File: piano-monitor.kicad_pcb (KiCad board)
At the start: 2 copper layers, 37.2 x 43 mm, 1 part

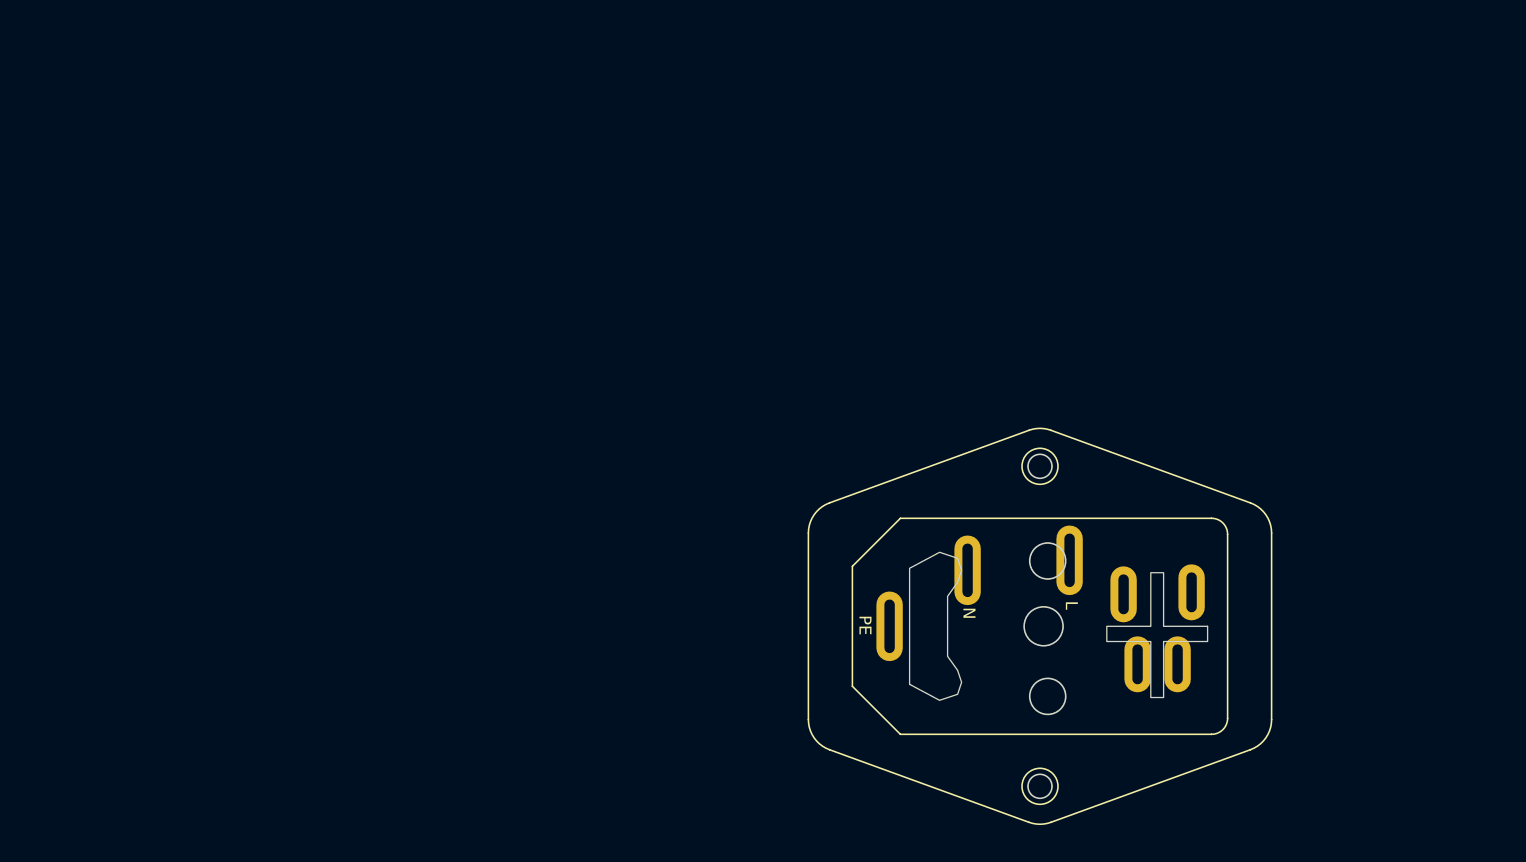
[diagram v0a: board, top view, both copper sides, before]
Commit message: Add tpa3110 footprint
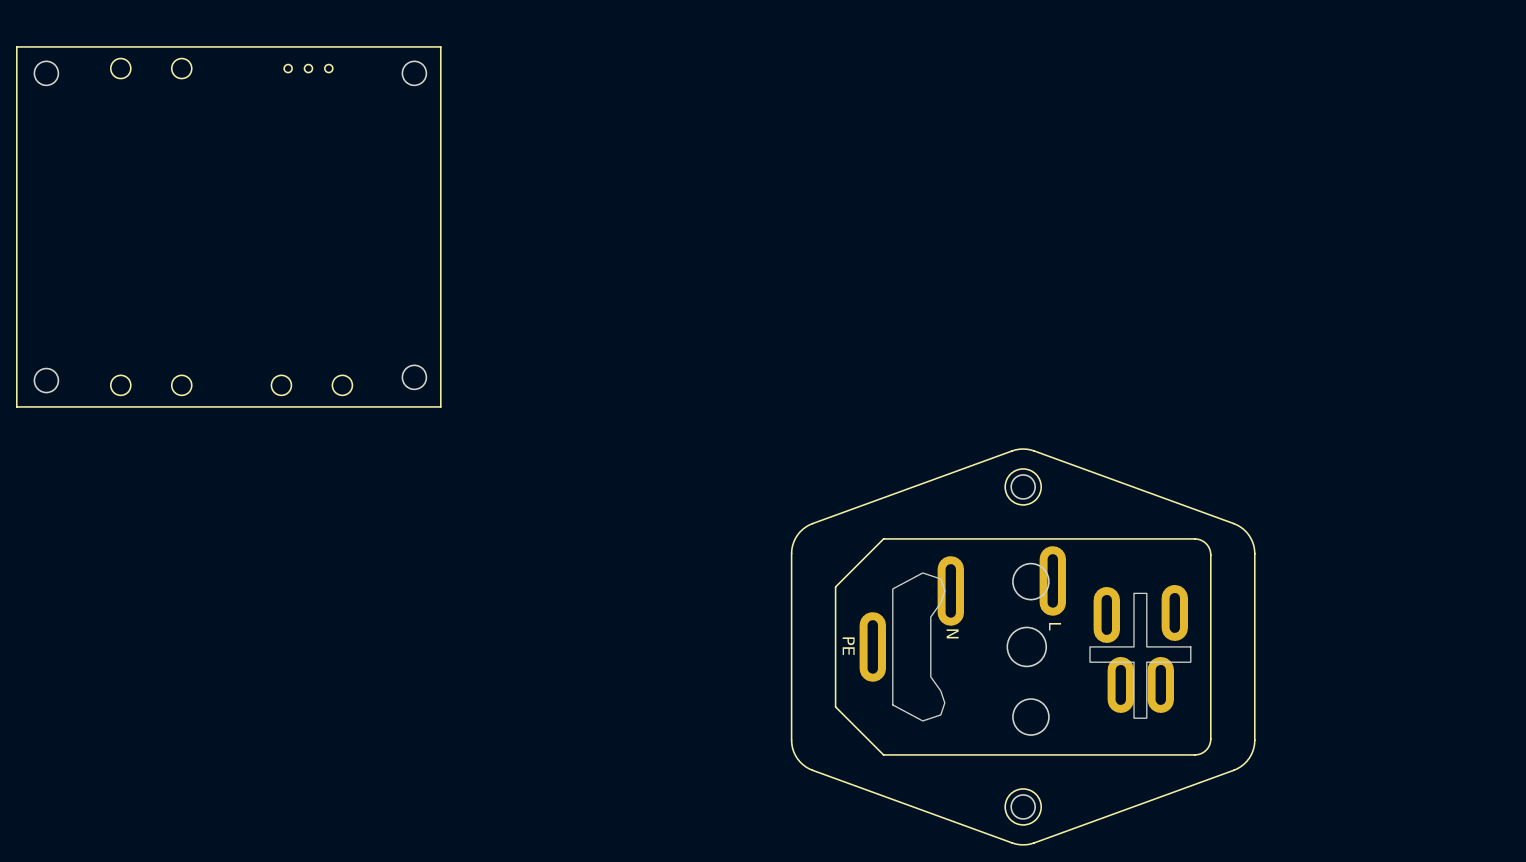
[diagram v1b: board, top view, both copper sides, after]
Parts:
- moved J1 3.33 mm to (224.2, 127.6)
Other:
- board size 37.2 x 43 mm -> 49 x 41.4 mm
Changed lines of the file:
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@@
 	(footprint "iec320-c14:iec320-c14"
 		(layer "F.Cu")
-		(at 226.25 125 -90)
+		(at 224.15 127.58 -90)
 		(property "Reference" "J1"
 			(at 0 -0.5 -90)
@@
 		)
 	)
+	(gr_line
+		(start 97.9 52.58)
+		(end 150.9 52.58)
+		(stroke
+			(width 0.2)
+			(type default)
+		)
+		(layer "F.SilkS")
+	)
+	(gr_circle
+		(center 118.52 55.28)
+		(end 119.77 55.28)
+		(stroke
+			(width 0.2)
+			(type default)
+		)
+		(fill none)
+		(layer "F.SilkS")
+	)
+	(gr_circle
+		(center 118.52 94.88)
+		(end 119.77 94.88)
+		(stroke
+			(width 0.2)
+			(type default)
+		)
+		(fill none)
+		(layer "F.SilkS")
+	)
+	(gr_line
+		(start 150.9 52.58)
+		(end 150.9 97.58)
+		(stroke
+			(width 0.2)
+			(type default)
+		)
+		(layer "F.SilkS")
+	)
+	(gr_circle
+		(center 136.9 55.28)
+		(end 137.4 55.28)
+		(stroke
+			(width 0.2)
+			(type default)
+		)
+		(fill none)
+		(layer "F.SilkS")
+	)
+	(gr_circle
+		(center 110.9 94.88)
+		(end 112.15 94.88)
+		(stroke
+			(width 0.2)
+			(type default)
+		)
+		(fill none)
+		(layer "F.SilkS")
+	)
+	(gr_circle
+		(center 131.82 55.28)
+		(end 132.32 55.28)
+		(stroke
+			(width 0.2)
+			(type default)
+		)
+		(fill none)
+		(layer "F.SilkS")
+	)
+	(gr_circle
+		(center 130.98 94.88)
+		(end 132.23 94.88)
+		(stroke
+			(width 0.2)
+			(type default)
+		)
+		(fill none)
+		(layer "F.SilkS")
+	)
+	(gr_circle
+		(center 138.6 94.88)
+		(end 139.85 94.88)
+		(stroke
+			(width 0.2)
+			(type default)
+		)
+		(fill none)
+		(layer "F.SilkS")
+	)
+	(gr_line
+		(start 150.9 97.58)
+		(end 97.9 97.58)
+		(stroke
+			(width 0.2)
+			(type default)
+		)
+		(layer "F.SilkS")
+	)
+	(gr_circle
+		(center 134.36 55.28)
+		(end 134.86 55.28)
+		(stroke
+			(width 0.2)
+			(type default)
+		)
+		(fill none)
+		(layer "F.SilkS")
+	)
+	(gr_circle
+		(center 124.4 75.08)
+		(end 124.41 75.08)
+		(stroke
+			(width 0.0001)
+			(type default)
+		)
+		(fill solid)
+		(layer "F.SilkS")
+	)
+	(gr_line
+		(start 97.9 97.58)
+		(end 97.9 52.58)
+		(stroke
+			(width 0.2)
+			(type default)
+		)
+		(layer "F.SilkS")
+	)
+	(gr_circle
+		(center 110.9 55.28)
+		(end 112.15 55.28)
+		(stroke
+			(width 0.2)
+			(type default)
+		)
+		(fill none)
+		(layer "F.SilkS")
+	)
+	(gr_circle
+		(center 147.6 93.88)
+		(end 149.1 93.88)
+		(stroke
+			(width 0.2)
+			(type default)
+		)
+		(fill none)
+		(layer "Edge.Cuts")
+	)
+	(gr_circle
+		(center 147.6 55.88)
+		(end 149.1 55.88)
+		(stroke
+			(width 0.2)
+			(type default)
+		)
+		(fill none)
+		(layer "Edge.Cuts")
+	)
+	(gr_circle
+		(center 101.6 94.28)
+		(end 103.1 94.28)
+		(stroke
+			(width 0.2)
+			(type default)
+		)
+		(fill none)
+		(layer "Edge.Cuts")
+	)
+	(gr_circle
+		(center 101.6 55.88)
+		(end 103.1 55.88)
+		(stroke
+			(width 0.2)
+			(type default)
+		)
+		(fill none)
+		(layer "Edge.Cuts")
+	)
 )

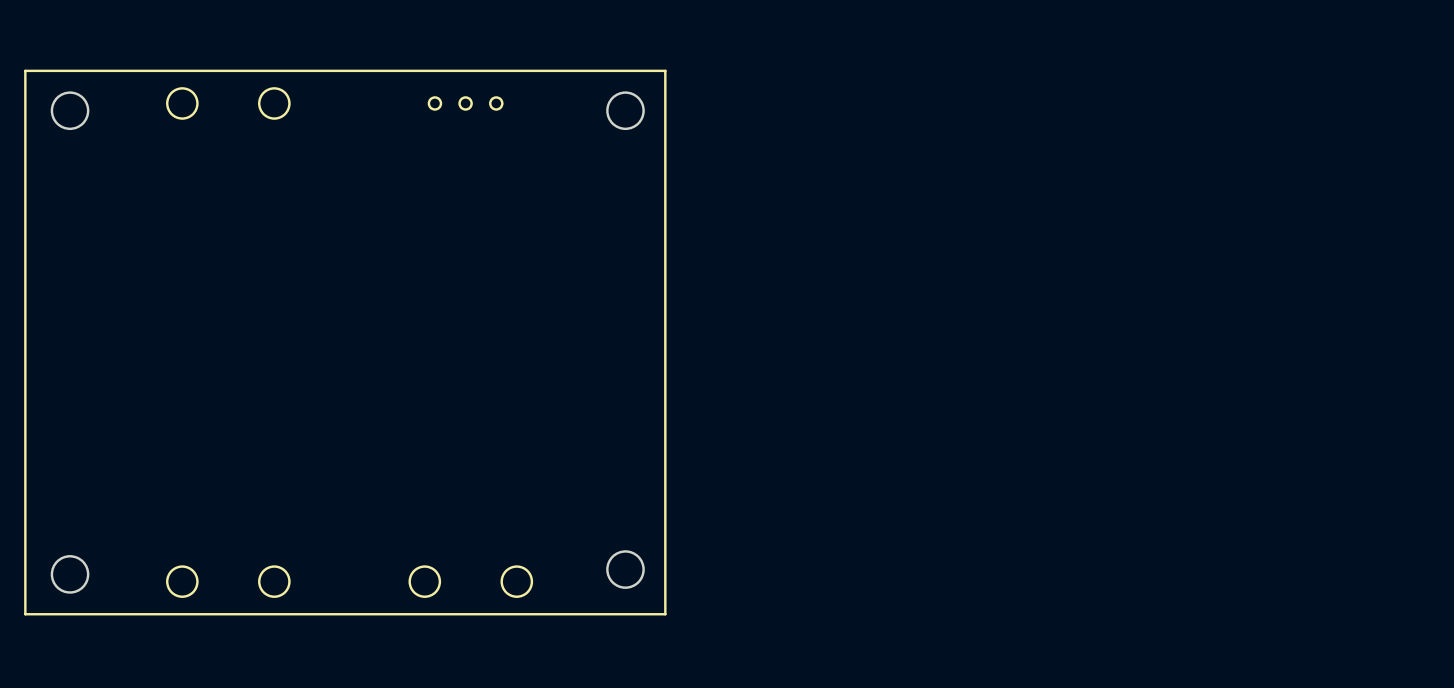
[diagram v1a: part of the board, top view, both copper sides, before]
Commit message: Add initial schematic
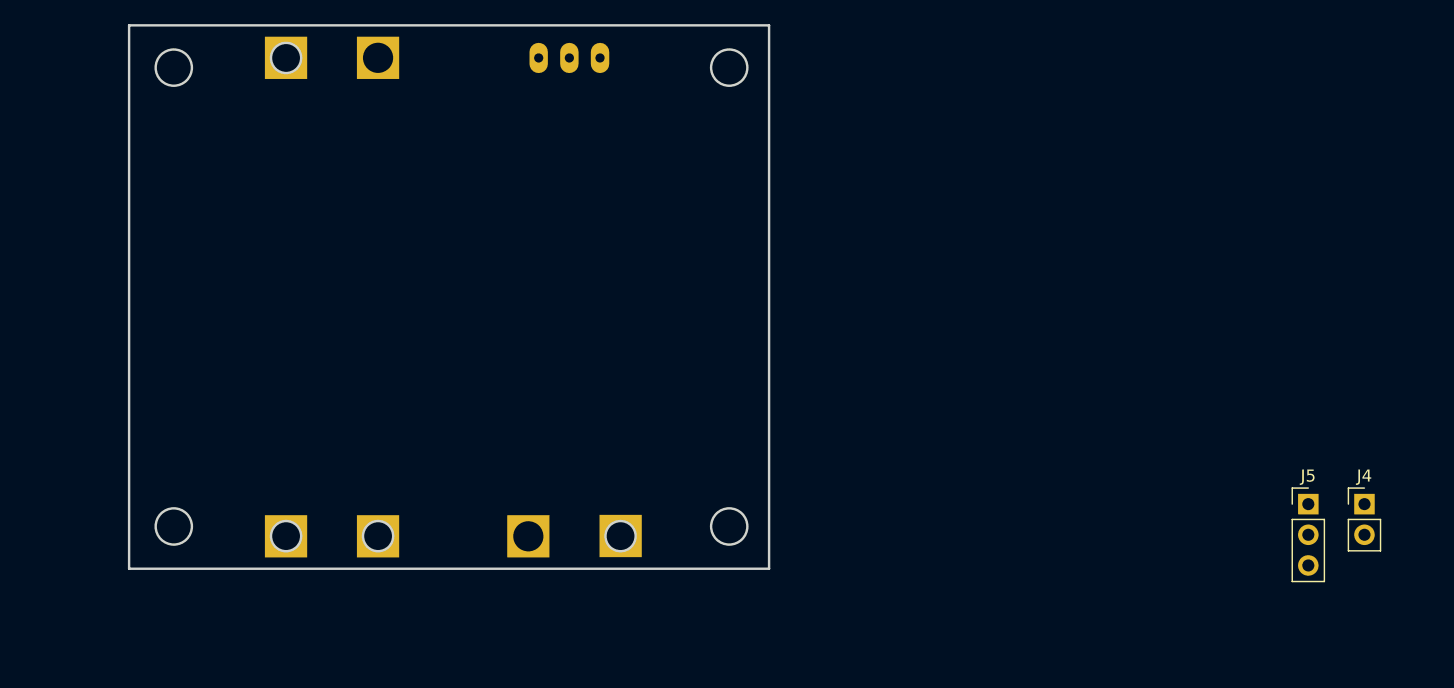
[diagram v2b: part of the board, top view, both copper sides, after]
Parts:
- added J4: DC, Connector_PinHeader_2.54mm:PinHeader_1x02_P2.54mm_Vertical, F.Cu at (208.8, 88.5)
- added J5: 230AC, Connector_PinHeader_2.54mm:PinHeader_1x03_P2.54mm_Vertical, F.Cu at (204.2, 88.5)
- added U1: ~, tpa3110:tpa3110, F.Cu at (133.0, 71.2)
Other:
- board size 49 x 41.4 mm -> 53 x 45 mm

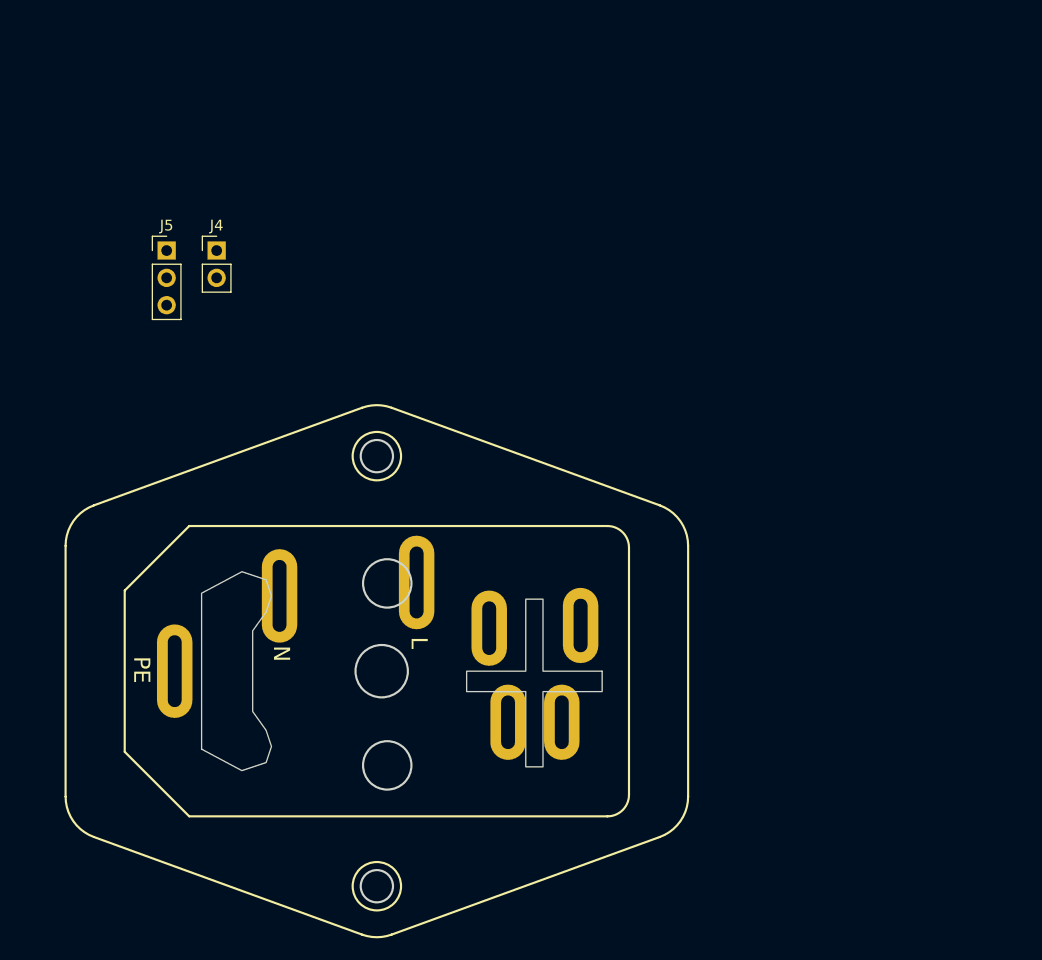
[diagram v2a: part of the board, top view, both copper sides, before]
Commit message: Update the C14 plug symbol and footprint
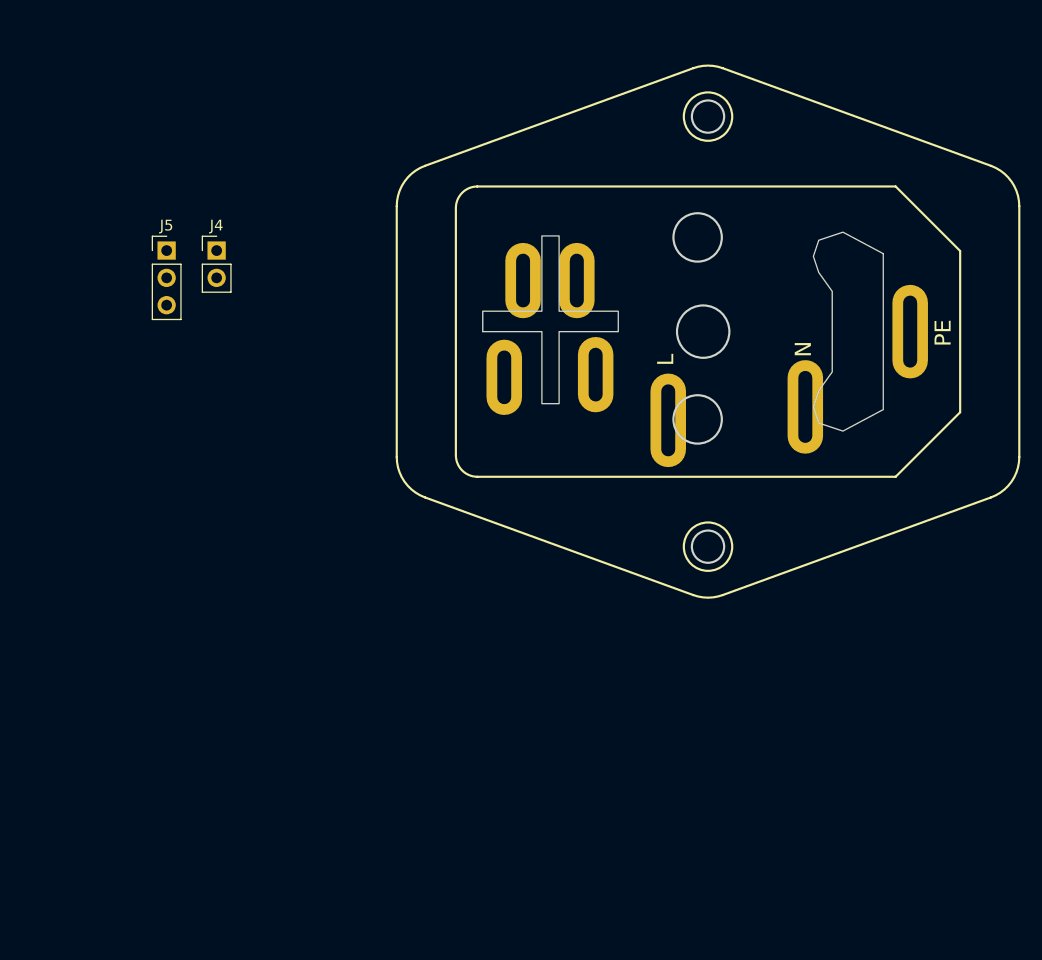
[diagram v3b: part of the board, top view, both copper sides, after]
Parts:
- moved J1 43.5 mm to (254.1, 96.0), turned to 90 degrees
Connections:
- J1 pad 1: Net-(J1-A) -> Net-(J1-B)
- J1 pad 2: Net-(J1-B) -> Net-(J1-A)

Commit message: Update PCB
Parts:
- added J17: ~, c14-outlet:c14-outlet, F.Cu at (204.6, 103.5)
- moved U1 34.7 mm to (154.1, 98.7)
- turned J1 to -90 degrees
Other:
- board size 53 x 45 mm -> 158 x 63.4 mm

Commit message: Update Schematic
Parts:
- removed J17: ~, c14-outlet:c14-outlet
- added J3: NCJ6FA-V, Connector_Audio:Jack_XLR-6.35mm_Neutrik_NCJ6FA-V_Vertical, F.Cu at (132.1, 113.2)
- added J6: ~, c14-outlet:c14-outlet, F.Cu at (209.6, 96.9)
- added J7: NCJ6FA-V, Connector_Audio:Jack_XLR-6.35mm_Neutrik_NCJ6FA-V_Vertical, F.Cu at (158.8, 113.8)
- moved J4 42.6 mm to (166.7, 95.2)
- moved U1 27.3 mm to (137.2, 77.2), turned to 180 degrees
- moved J5 26.1 mm to (206.5, 62.5), turned to 90 degrees
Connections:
- U1 pad 1: Net-(J3-PadT) -> T1
- U1 pad 2: Net-(J6-PadT) -> T2
- U1 pad 3: Net-(U1--) -> S1
- U1 pad 5: GND -> S1
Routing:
- net S1: track 0.00 -> 44.7 mm
- net T2: track 0.00 -> 38.2 mm
- net T1: track 0.00 -> 37.4 mm
- net R2: track 0.00 -> 8.19 mm
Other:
- board size 158 x 63.4 mm -> 173.6 x 79 mm

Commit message: Add some traces
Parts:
- removed J5: 230AC, Connector_PinHeader_2.54mm:PinHeader_1x03_P2.54mm_Vertical
- moved U1 1.91 mm to (139.0, 77.8)
- moved J3 0.82 mm to (132.7, 113.9)
- turned J6 to -90 degrees
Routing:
- net L: track 0.00 -> 67.8 mm
- net N: track 0.00 -> 67.4 mm
- net S1: track 44.7 -> 84.0 mm
- net Net-(J1-B): track 0.00 -> 37.4 mm
- net +24V: track 0.00 -> 16.3 mm
- net R2: track 8.19 -> 0.00 mm
- net Net-(J1-A): track 0.00 -> 7.98 mm
- net T2: track 38.2 -> 35.6 mm
- added copper zone on B.Cu, net Earth
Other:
- board size 173.6 x 79 mm -> 169.1 x 74.8 mm
